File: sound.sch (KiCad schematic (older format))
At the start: 13 parts, among them IC1 MAX4466EXK+T

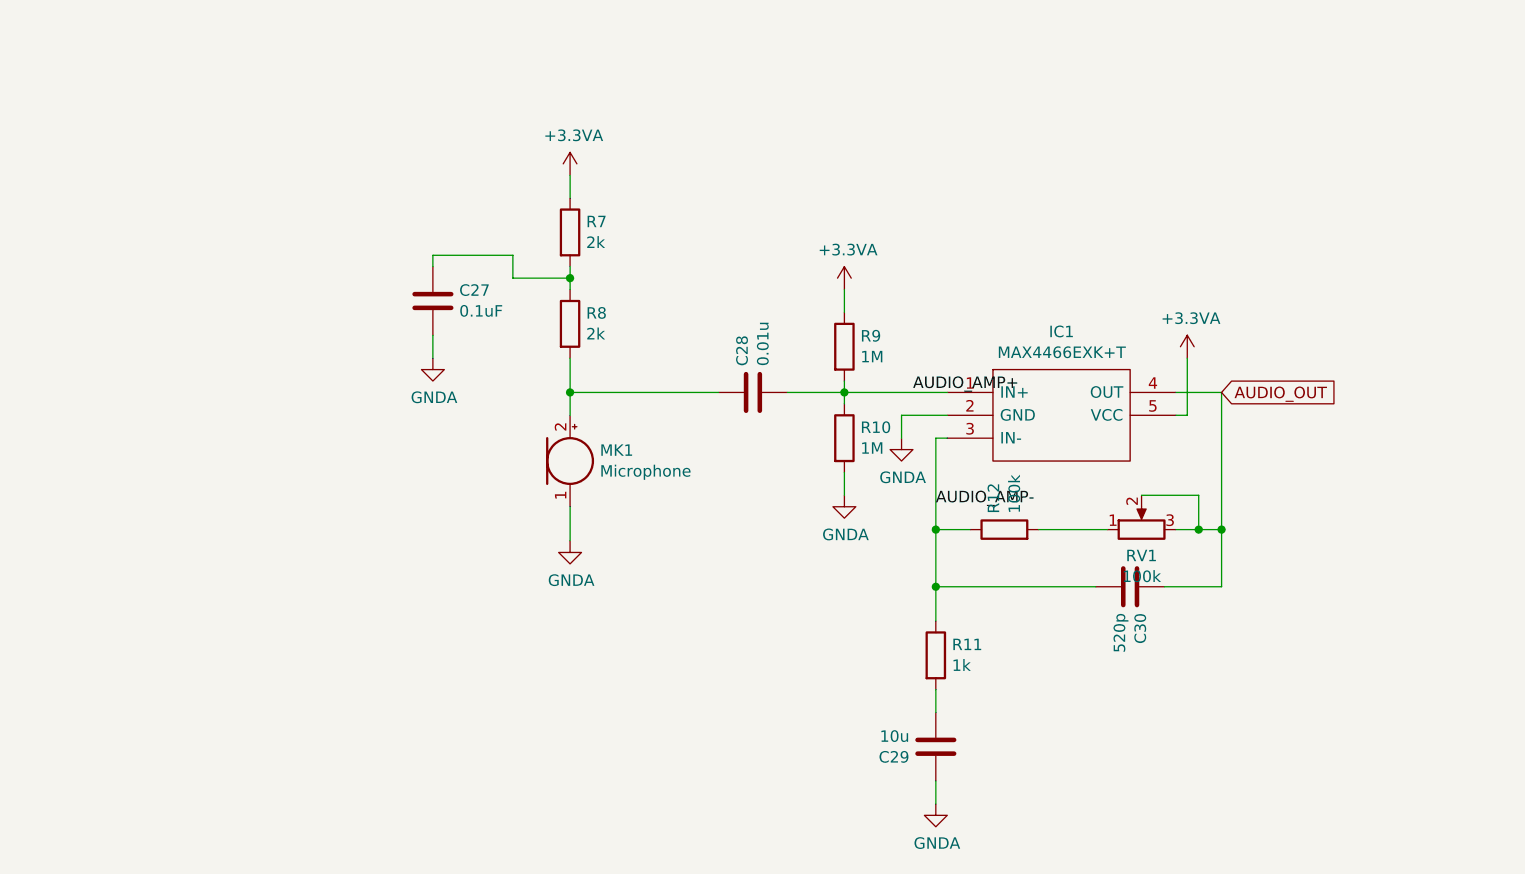
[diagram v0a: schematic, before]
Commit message: Added a 9-dof IMU, however it cant be sourced because of chips. But it is a start.
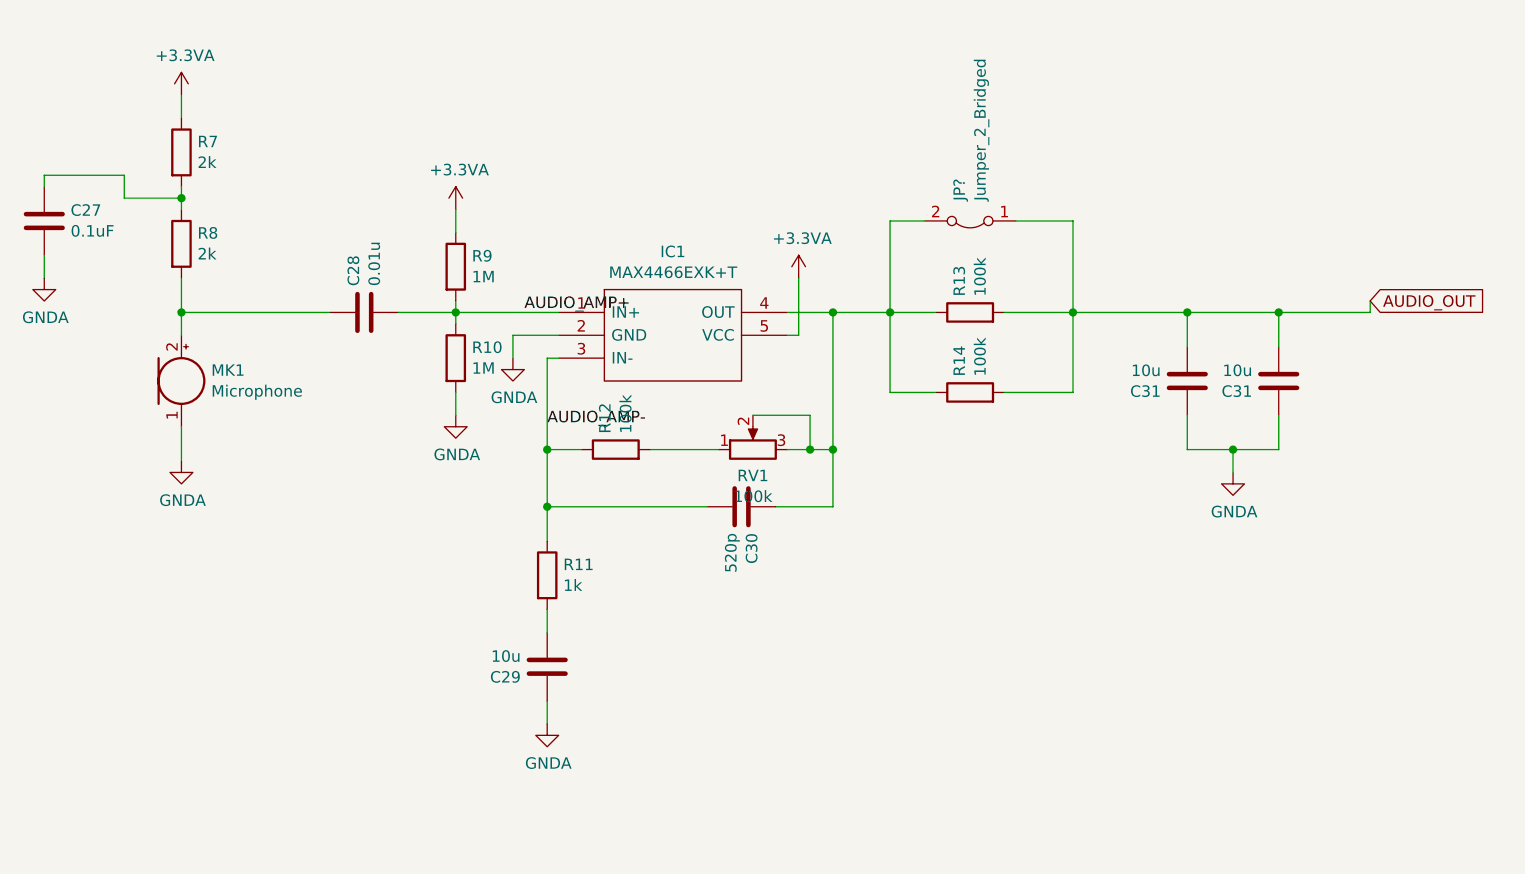
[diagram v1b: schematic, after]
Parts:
- added C31 (x2): 10u, Capacitor_SMD:C_0603_1608Metric, symbol Device:C
- added JP?: Jumper_2_Bridged, Jumper:SolderJumper-2_P1.3mm_Open_TrianglePad1.0x1.5mm, symbol Jumper:Jumper_2_Bridged
- added R13, R14: 100k, Resistor_SMD:R_0603_1608Metric_Pad0.98x0.95mm_HandSolder, symbol Device:R
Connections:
- net AUDIO_OUT: now also C31.2, C31.2, JP?.1 (A), R13.2, R14.2; no longer C30.1, IC1.4 (OUT), RV1.2, RV1.3
- net GNDA: now also C31.1, C31.1
- new net: C30.1, IC1.4 (OUT), JP?.2 (B), R13.1, R14.1, RV1.2, RV1.3
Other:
- moved on the sheet: C27, C28, C29, C30, IC1, MK1, R10, R11, R12, R7, R8, R9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
